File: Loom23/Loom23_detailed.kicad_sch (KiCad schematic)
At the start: 7 parts

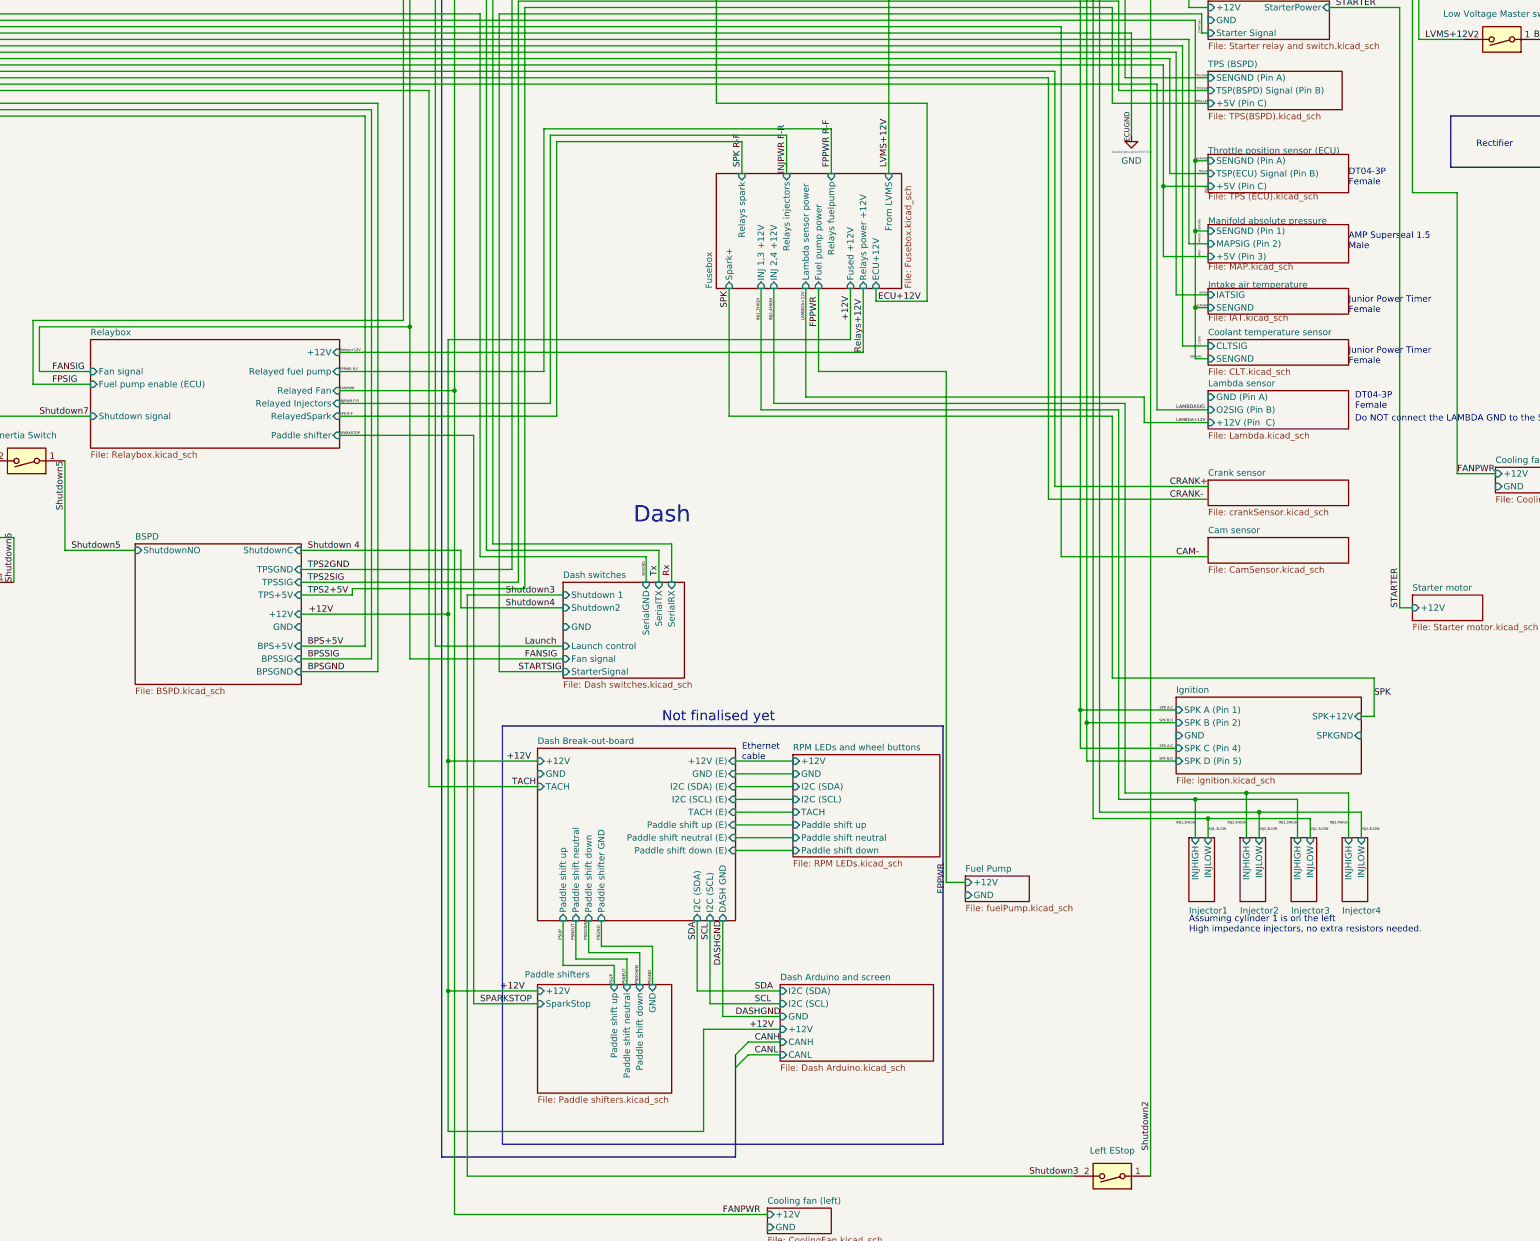
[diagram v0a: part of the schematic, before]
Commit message: Added paddle shifter PCB and the relays.
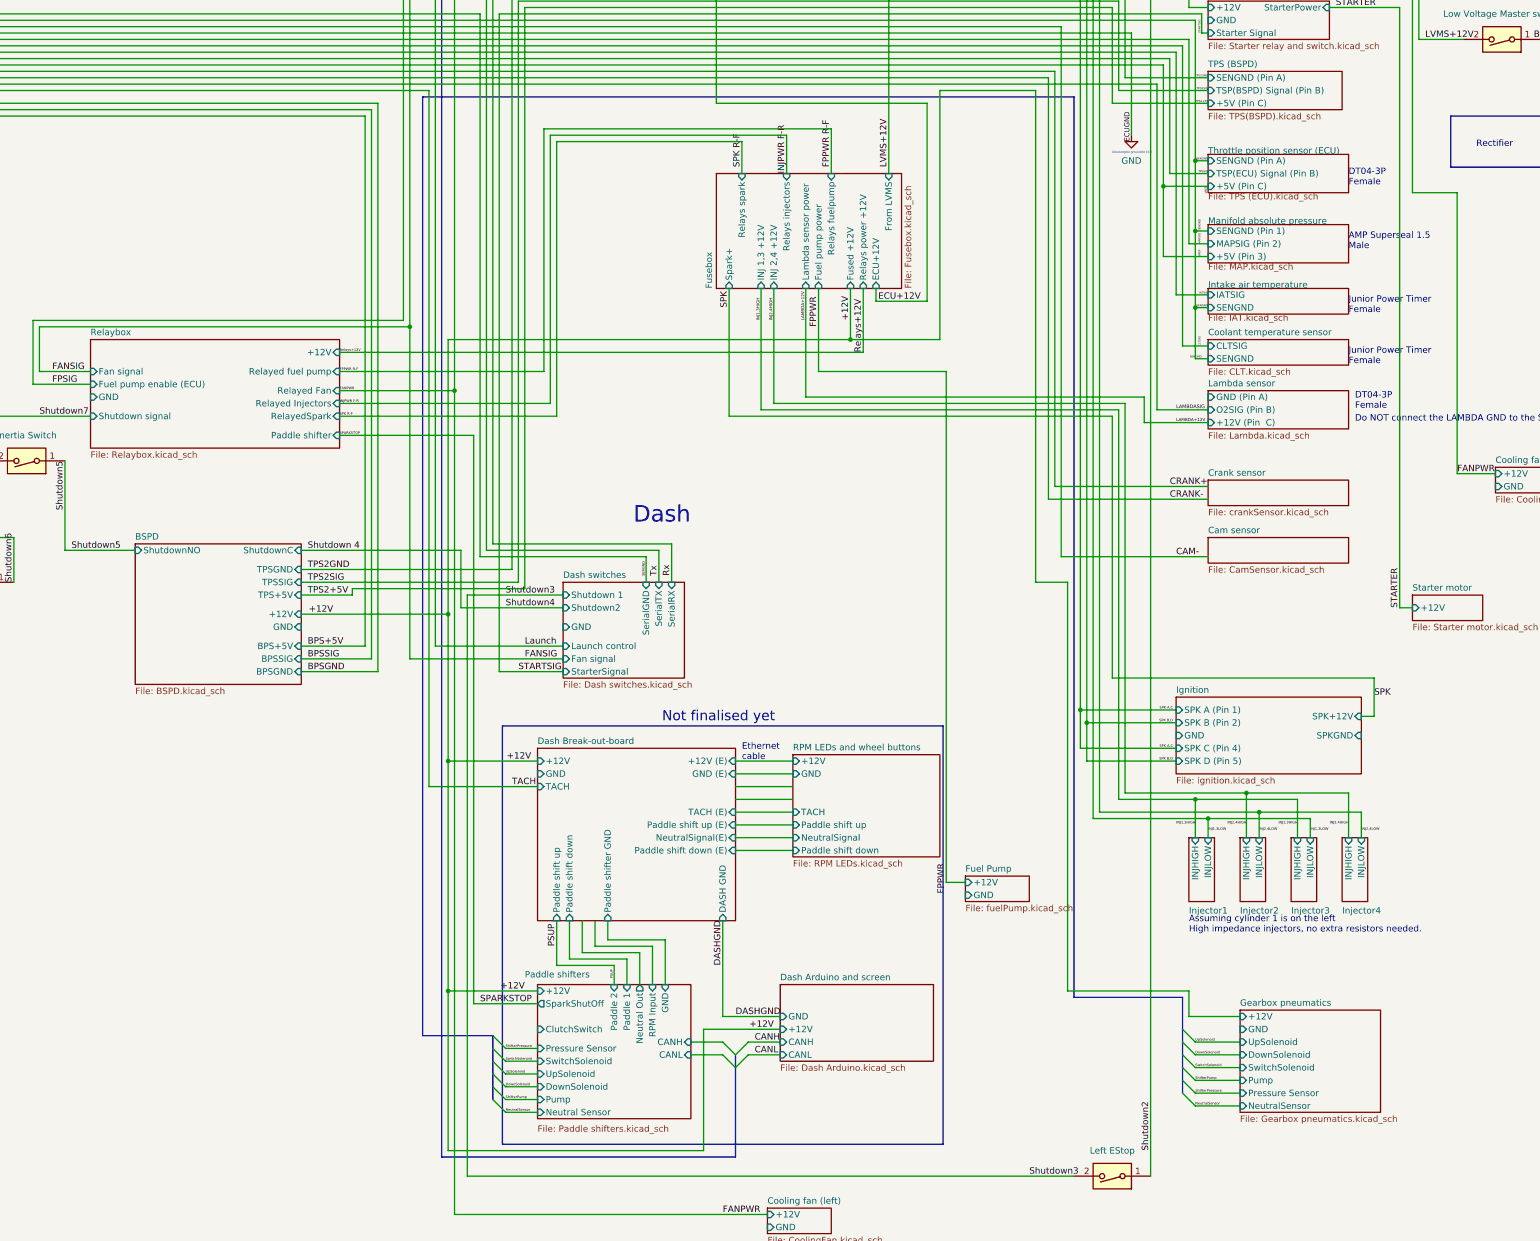
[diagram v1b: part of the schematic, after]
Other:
- added sheet Gearbox pneumatics (Gearbox pneumatics.kicad_sch)
- sheet Dash Arduino and screen ports: added none; removed I2C (SCL), I2C (SDA)
- sheet Dash Break-out-board ports: added NeutralSignal(E); removed I2C (SCL), I2C (SCL) (E), I2C (SDA), I2C (SDA) (E), Paddle shift neutral, Paddle shift neutral (E)
- sheet Paddle shifters ports: added CANH, CANL, ClutchSwitch, DownSolenoid, Neutral Out, Neutral Sensor, Paddle 1, Paddle 2, Pressure Sensor, Pump, RPM Input, SparkShutOff, SwitchSolenoid, UpSolenoid; removed Paddle shift down, Paddle shift neutral, Paddle shift up, SparkStop
- sheet RPM LEDs and wheel buttons ports: added NeutralSignal; removed I2C (SCL), I2C (SDA), Paddle shift neutral
- sheet Relaybox ports: added GND; removed none

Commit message: Added brake light
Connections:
- net LVMS+12V renamed LVMS +12V
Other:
- removed sheet Telemetry
- sheet Dash Break-out-board ports: added CANH, CANL; removed none
- sheet RPM LEDs and wheel buttons ports: added CANH, CANL; removed none
- note added: "Brake Light"
- note added: "Brake line pressure sensor"
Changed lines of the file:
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@@
   (junction (at 375.92 102.87) (diameter 0) (color 0 0 0 0)
   )
-  (junction (at 55.88 115.57) (diameter 0) (color 0 0 0 0)
-  )
   (junction (at 226.06 130.81) (diameter 0) (color 0 0 0 0)
   )
@@
   )
   (junction (at 407.67 63.5) (diameter 0) (color 0 0 0 0)
+  )
+  (junction (at 321.31 63.5) (diameter 0) (color 0 0 0 0)
   )
   (junction (at 360.68 209.55) (diameter 0) (color 0 0 0 0)
@@
     (stroke (width 0) (type default) (color 0 0 0 0))
   )
-  (bus (pts (xy 43.18 93.98) (xy 55.88 93.98))
-    (stroke (width 0) (type default) (color 0 0 0 0))
-  )
   (wire (pts (xy 245.11 284.48) (xy 251.46 284.48))
     (stroke (width 0) (type default) (color 0 0 0 0))
@@
     (stroke (width 0) (type default) (color 0 0 0 0))
   )
+  (polyline (pts (xy 467.36 73.66) (xy 476.25 73.66))
+    (stroke (width 0) (type default) (color 0 0 0 0))
+  )
   (wire (pts (xy 360.68 60.96) (xy 360.68 209.55))
     (stroke (width 0) (type default) (color 255 0 0 1))
@@
     (stroke (width 0) (type default) (color 0 0 0 0))
   )
+  (polyline (pts (xy 467.36 73.66) (xy 467.36 81.28))
+    (stroke (width 0) (type default) (color 0 0 0 0))
+  )
   (wire (pts (xy 461.01 73.66) (xy 461.01 81.28))
     (stroke (width 0) (type default) (color 0 0 0 0))
@@
   )
   (bus (pts (xy 242.57 276.86) (xy 242.57 279.4))
+    (stroke (width 0) (type default) (color 0 0 0 0))
+  )
+  (polyline (pts (xy 476.25 73.66) (xy 476.25 81.28))
     (stroke (width 0) (type default) (color 0 0 0 0))
   )
@@
     (stroke (width 0) (type default) (color 0 0 0 0))
   )
+  (wire (pts (xy 321.31 46.99) (xy 327.66 46.99))
+    (stroke (width 0) (type default) (color 0 0 0 0))
+  )
   (wire (pts (xy 304.8 123.19) (xy 304.8 144.78))
     (stroke (width 0) (type default) (color 0 0 0 0))
@@
     (stroke (width 0) (type default) (color 0 0 0 0))
   )
-  (bus (pts (xy 56.515 115.57) (xy 55.88 115.57))
-    (stroke (width 0) (type default) (color 0 0 0 0))
-  )
   (polyline (pts (xy 452.12 99.06) (xy 452.12 88.9))
     (stroke (width 0) (type default) (color 0 0 0 0))
@@
   (wire (pts (xy 415.29 227.33) (xy 415.29 232.41))
     (stroke (width 0) (type default) (color 0 255 0 1))
+  )
+  (wire (pts (xy 367.03 41.91) (xy 443.23 41.91))
+    (stroke (width 0) (type default) (color 0 0 0 0))
   )
   (wire (pts (xy 62.23 233.68) (xy 71.12 233.68))
@@
     (stroke (width 0) (type default) (color 0 0 0 0))
   )
+  (polyline (pts (xy 340.36 49.53) (xy 340.36 44.45))
+    (stroke (width 0) (type default) (color 0 0 0 0))
+  )
   (wire (pts (xy 365.76 86.36) (xy 365.76 67.31))
     (stroke (width 0) (type default) (color 0 0 0 0))
@@
     (stroke (width 0) (type default) (color 0 0 255 1))
   )
+  (wire (pts (xy 443.23 41.91) (xy 443.23 59.69))
+    (stroke (width 0) (type default) (color 0 0 0 0))
+  )
   (bus (pts (xy 379.73 278.13) (xy 379.73 280.67))
     (stroke (width 0) (type default) (color 0 0 0 0))
@@
     (stroke (width 0) (type default) (color 0 0 255 1))
   )
+  (wire (pts (xy 340.36 46.99) (xy 367.03 46.99))
+    (stroke (width 0) (type default) (color 0 0 0 0))
+  )
   (wire (pts (xy 355.6 71.12) (xy 355.6 176.53))
     (stroke (width 0) (type default) (color 0 255 0 1))
@@
   )
   (wire (pts (xy 248.92 67.31) (xy 248.92 182.88))
+    (stroke (width 0) (type default) (color 0 0 0 0))
+  )
+  (polyline (pts (xy 327.66 44.45) (xy 327.66 49.53))
     (stroke (width 0) (type default) (color 0 0 0 0))
   )
@@
     (stroke (width 0) (type default) (color 0 0 0 0))
   )
+  (wire (pts (xy 367.03 46.99) (xy 367.03 41.91))
+    (stroke (width 0) (type default) (color 0 0 0 0))
+  )
   (wire (pts (xy 245.11 276.86) (xy 251.46 276.86))
     (stroke (width 0) (type default) (color 0 0 0 0))
   )
+  (wire (pts (xy 443.23 59.69) (xy 471.17 59.69))
+    (stroke (width 0) (type default) (color 0 0 0 0))
+  )
   (wire (pts (xy 434.34 160.02) (xy 434.34 104.14))
     (stroke (width 0) (type default) (color 0 0 0 0))
@@
   )
   (wire (pts (xy 212.09 143.51) (xy 234.95 143.51))
+    (stroke (width 0) (type default) (color 0 0 0 0))
+  )
+  (polyline (pts (xy 327.66 44.45) (xy 340.36 44.45))
     (stroke (width 0) (type default) (color 0 0 0 0))
   )
@@
     (stroke (width 0) (type default) (color 0 0 0 0))
   )
+  (wire (pts (xy 321.31 63.5) (xy 321.31 46.99))
+    (stroke (width 0) (type default) (color 0 0 0 0))
+  )
   (wire (pts (xy 92.71 228.6) (xy 92.71 78.74))
     (stroke (width 0) (type default) (color 0 0 0 0))
@@
   )
   (wire (pts (xy 214.63 184.15) (xy 214.63 182.88))
+    (stroke (width 0) (type default) (color 0 0 0 0))
+  )
+  (wire (pts (xy 471.17 59.69) (xy 471.17 73.66))
     (stroke (width 0) (type default) (color 0 0 0 0))
   )
@@
     (stroke (width 0) (type default) (color 0 0 0 0))
   )
+  (polyline (pts (xy 327.66 49.53) (xy 340.36 49.53))
+    (stroke (width 0) (type default) (color 0 0 0 0))
+  )
   (wire (pts (xy 204.47 196.85) (xy 218.44 196.85))
     (stroke (width 0) (type default) (color 0 0 0 0))
@@
     (stroke (width 0) (type default) (color 0 255 0 1))
   )
-  (bus (pts (xy 55.88 93.98) (xy 55.88 115.57))
-    (stroke (width 0) (type default) (color 0 0 0 0))
-  )
   (wire (pts (xy 381 67.31) (xy 381 62.23))
     (stroke (width 0) (type default) (color 0 0 0 0))
@@
   (wire (pts (xy 359.41 207.01) (xy 378.46 207.01))
     (stroke (width 0) (type default) (color 0 255 0 1))
+  )
+  (polyline (pts (xy 476.25 81.28) (xy 467.36 81.28))
+    (stroke (width 0) (type default) (color 0 0 0 0))
   )
   (wire (pts (xy 240.03 176.53) (xy 273.05 176.53))
@@
     (stroke (width 0) (type default) (color 0 0 255 1))
   )
-  (bus (pts (xy 45.72 115.57) (xy 55.88 115.57))
+  (bus (pts (xy 45.72 115.57) (xy 56.515 115.57))
     (stroke (width 0) (type default) (color 0 0 0 0))
   )
@@
     (effects (font (size 2 2)) (justify left bottom))
   )
+  (text "Brake line \npressure sensor" (at 327.66 44.45 0)
+    (effects (font (size 1.27 1.27)) (justify left bottom))
+  )
+  (text "Brake Light\n" (at 477.52 78.74 0)
+    (effects (font (size 1.27 1.27)) (justify left bottom))
+  )
   (text "Junior Power Timer\nFemale\n" (at 412.75 128.27 0)
     (effects (font (size 1.27 1.27)) (justify left bottom))
@@
     (effects (font (size 1.27 1.27)) (justify left bottom))
   )
-  (text "CAN Bus" (at 46.99 88.9 0)
+  (text "CAN Bus" (at 43.18 109.22 0)
     (effects (font (size 2.27 2.27)) (justify left bottom))
   )
@@
     (effects (font (size 0.5 0.5)) (justify left bottom))
   )
+  (label "Brake light" (at 341.63 46.99 0)
+    (effects (font (size 1.27 1.27)) (justify left bottom))
+  )
   (label "SENGND" (at 384.81 127 180)
     (effects (font (size 0.4 0.4)) (justify right bottom))
@@
     (effects (font (size 1.27 1.27)) (justify left bottom))
   )
+  (label "LVMS +12V" (at 326.39 46.99 180)
+    (effects (font (size 0.6 0.6)) (justify right bottom))
+  )
   (label "Relays+12V" (at 212.09 135.89 0)
     (effects (font (size 0.5 0.5)) (justify left bottom))
@@
   (label "INJ2,4LOW" (at 415.29 231.14 0)
     (effects (font (size 0.5 0.5)) (justify left bottom))
+  )
+  (label "Brake light" (at 471.17 71.12 0)
+    (effects (font (size 1.27 1.27)) (justify left bottom))
   )
   (label "BPSSIG" (at 54.61 264.16 0)
@@
       (effects (font (size 1.27 1.27)) (justify right))
     )
+    (pin "CANH" input (at 290.83 222.25 0)
+      (effects (font (size 1.27 1.27)) (justify right))
+    )
+    (pin "CANL" input (at 290.83 224.79 0)
+      (effects (font (size 1.27 1.27)) (justify right))
+    )
   )
   (sheet (at 381 232.41) (size 5.08 12.7)
@@
     )
   )
-  (sheet (at 30.48 92.71) (size 12.7 3.81) (fields_autoplaced)
-    (stroke (width 0.1524) (type solid) (color 0 0 0 0))
-    (fill (color 0 0 0 0.0000))
-    (property "Sheet name" "Telemetry" (id 0) (at 30.48 91.9984 0)
-      (effects (font (size 1.27 1.27)) (justify left bottom))
-    )
-    (property "Sheet file" "Telemetry.kicad_sch" (id 1) (at 30.48 97.1046 0)
-      (effects (font (size 1.27 1.27)) (justify left top))
-    )
-  )
   (sheet (at 384.81 66.04) (size 24.13 7.62) (fields_autoplaced)
     (stroke (width 0.1524) (type solid) (color 0 0 0 0))
@@
     )
     (pin "NeutralSignal" input (at 302.26 232.41 180)
+      (effects (font (size 1.27 1.27)) (justify left))
+    )
+    (pin "CANL" input (at 302.26 224.79 180)
+      (effects (font (size 1.27 1.27)) (justify left))
+    )
+    (pin "CANH" input (at 302.26 222.25 180)
       (effects (font (size 1.27 1.27)) (justify left))
     )
@@
     (path "/f6d62036-1353-44c1-8bdb-c554d032f03c" (page "17"))
     (path "/10890e7c-b700-45d3-80f8-41487eb0e501" (page "18"))
-    (path "/893d034b-5e7b-449a-8d64-c5dd8cd1d47b" (page "20"))
     (path "/e7e35a98-fa36-447d-8c61-939a2107a6a8" (page "21"))
     (path "/1d4732f1-f7ed-413e-8ddf-5b2c37a3c5df" (page "22"))
